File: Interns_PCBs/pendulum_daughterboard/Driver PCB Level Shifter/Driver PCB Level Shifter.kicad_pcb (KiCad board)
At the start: 2 copper layers, 69.2 x 54 mm, 69 parts, among them IC1 MAX9928FAUA+, J1 AVR-ISP-6, J2 Coil, J3 DRIVE_5V, J4 Conn_01x04, J5 DRIVE_GND, Q1 BC858W, Q2 BD911, SW1 SW_Push, U1 4081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

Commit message: Penduino Daughterboard with Level Shifter
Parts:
- removed EC3, EC4: 10u, Capacitor_SMD:CP_Elec_4x5.4
- removed J3: DRIVE_5V, Connector_Pin:Pin_D1.3mm_L11.0mm
- removed J5: DRIVE_GND, Connector_Pin:Pin_D1.3mm_L11.0mm
- added R10: 10K, Resistor_SMD:R_0805_2012Metric_Pad1.20x1.40mm_HandSolder, F.Cu at (89.9, 94.5)
- added R11: 10K, Resistor_SMD:R_0805_2012Metric_Pad1.20x1.40mm_HandSolder, F.Cu at (94.3, 85.7)
- added R12: 10K, Resistor_SMD:R_0805_2012Metric_Pad1.20x1.40mm_HandSolder, F.Cu at (89.9, 91.5)
- added R14: 10K, Resistor_SMD:R_0805_2012Metric_Pad1.20x1.40mm_HandSolder, F.Cu at (94.7, 88.6)
- U6: value AMS1117-3.3 -> SN74LVC2T45DCUR; footprint Package_TO_SOT_SMD:SOT-223-3_TabPin2 -> Package_SO:VSSOP-8_2.4x2.1mm_P0.5mm
- moved U6 41.6 mm to (84.8, 94.2)
- moved EC1 36.0 mm to (88.1, 87.1)
- moved EC2 34.8 mm to (78.2, 95.3), turned to 0 degrees
- moved U5 9.43 mm to (122.4, 103.8)
- renumbered D1_GN to D1, D2_OR to D2, D3_RD to D3, D5_RD to D5
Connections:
- EC2 pad 1: D_3.3V -> 3.3V
- J1 pad 1: LOAD_INPUT -> LOAD
- J1 pad 3: DRIVE_INPUT -> DRIVE
- U5 pad 2: D_3.3V -> 3.3V
- U6 pad 1: DRIVE_GND -> 3.3V
- U6 pad 2: PEND_3.3V -> DRIVE
- U6 pad 3: /Linear Voltage Conversion/DRIVE_5V -> LOAD
- U7 pad 6: LOAD_INPUT -> LOAD
- U7 pad 7: DRIVE_INPUT -> DRIVE
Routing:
- net DRIVE_INPUT: track 81.4 -> 2.54 mm, vias 3 -> 0
- net LOAD_INPUT: track 74.1 -> 0.00 mm, vias 2 -> 0
- net D_5V: track 41.8 -> 0.00 mm, vias 2 -> 0
- net DRIVE_GND: track 182.9 -> 141.9 mm, vias 7 -> 5
- net D_3.3V: track 93.3 -> 61.8 mm, vias 8 -> 6
- net LOAD: track 0.00 -> 30.9 mm, vias 0 -> 1
- net /Linear Voltage Conversion/DRIVE_5V: track 24.7 -> 0.00 mm
- net PEND_3.3V: track 112.1 -> 90.0 mm
- net D_GND: track 118.9 -> 107.7 mm, vias 10 -> 7
- net STUDENT_ENABLE: track 52.9 -> 51.5 mm
- net Net-(R26-Pad1): track 13.1 -> 12.0 mm
- net Net-(R30-Pad1): track 13.0 -> 12.0 mm
- net Net-(R29-Pad1): track 34.2 -> 33.4 mm
- net Net-(R28-Pad1): track 34.4 -> 33.8 mm
- net Net-(R27-Pad1): track 39.1 -> 38.5 mm
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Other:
- board text removed: "DRIVE_5V"
- board text removed: "DRIVE_GND"
- board text removed: "D_3.3V"
- board text removed: "PEND_3.3V"

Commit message: Pin update
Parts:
- added C10: 100nF, Capacitor_SMD:C_0805_2012Metric_Pad1.18x1.45mm_HandSolder, F.Cu at (130.4, 109.8)
- added C11: 100nF, Capacitor_SMD:C_0805_2012Metric_Pad1.18x1.45mm_HandSolder, F.Cu at (117.4, 110.2)
- moved U6 41.3 mm to (124.4, 106.0), turned to 180 degrees
- moved R12 41.1 mm to (126.3, 110.7)
- moved EC2 36.3 mm to (110.0, 112.9)
- moved R10 35.9 mm to (121.9, 110.7), turned to 180 degrees
- moved R14 34.2 mm to (126.7, 100.6), turned to 180 degrees
- moved R11 30.3 mm to (118.9, 103.4)
- moved EC1 24.3 mm to (110.0, 97.6), turned to 180 degrees
- moved U5 12.5 mm to (110.0, 105.5)
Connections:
- A1 pad 19: LOAD_INPUT -> DRIVE_INPUT
- A1 pad 27: DRIVE_INPUT -> LOAD_INPUT
- A1 pad 28: DRIVE_INPUT -> LOAD_INPUT
- A1 pad 5: D_5V -> 5V
- A1 pad 7: D_GND -> GND
- C1 pad 1: PEND_3.3V -> 5V
- C1 pad 2: DRIVE_GND -> GND
- C2 pad 1: PEND_3.3V -> 5V
- C2 pad 2: DRIVE_GND -> GND
- C3 pad 1: PEND_3.3V -> 5V
- C3 pad 2: DRIVE_GND -> GND
- C4 pad 1: D_3.3V -> 5V
- C4 pad 2: D_GND -> GND
- C5 pad 1: D_3.3V -> 5V
- C5 pad 2: D_GND -> GND
- C6 pad 1: D_3.3V -> 5V
- C6 pad 2: D_GND -> GND
- C7 pad 1: D_3.3V -> 5V
- C7 pad 2: D_GND -> GND
- C8 pad 1: PEND_3.3V -> 5V
- C8 pad 2: DRIVE_GND -> GND
- C9 pad 1: PEND_3.3V -> 5V
- C9 pad 2: DRIVE_GND -> GND
- D4 pad 1: DRIVE_GND -> GND
- D5 pad 1: DRIVE_GND -> GND
- EC1 pad 1: D_5V -> 5V
- EC1 pad 2: D_GND -> GND
- EC2 pad 2: D_GND -> GND
- J1 pad 2: PEND_3.3V -> 5V
- J1 pad 6: DRIVE_GND -> GND
- J2 pad 1: DRIVE_GND -> GND
- J4 pad 1: D_GND -> GND
- NT2 pad 2: PEND_3.3V -> 5V
- NT3 pad 2: DRIVE_GND -> GND
- Q1 pad 2: PEND_3.3V -> 5V
- Q2 pad 3: DRIVE_GND -> GND
- R1 pad 1: D_GND -> GND
- R10 pad 1: D_GND -> GND
- R11 pad 2: D_GND -> GND
- R12 pad 1: D_GND -> GND
- R13 pad 2: D_GND -> GND
- R14 pad 2: D_GND -> GND
- R15 pad 2: D_GND -> GND
- R17 pad 2: D_GND -> GND
- R18 pad 2: D_GND -> GND
- R19 pad 2: D_GND -> GND
- R2 pad 1: D_GND -> GND
- R20 pad 2: D_GND -> GND
- R21 pad 2: D_GND -> GND
- R22 pad 2: D_GND -> GND
- R23 pad 2: D_GND -> GND
- R24 pad 2: D_GND -> GND
- R25 pad 2: D_GND -> GND
- R26 pad 2: D_GND -> GND
- R27 pad 2: D_GND -> GND
- R28 pad 2: D_GND -> GND
- R29 pad 2: D_GND -> GND
- R3 pad 1: D_GND -> GND
- R30 pad 2: D_GND -> GND
- R31 pad 2: D_GND -> GND
- R32 pad 2: D_GND -> GND
- R33 pad 2: D_GND -> GND
- R6 pad 2: PEND_3.3V -> 5V
- R9 pad 2: D_GND -> GND
- SW1 pad 1: DRIVE_GND -> GND
- U1 pad 14: D_3.3V -> 5V
- U1 pad 7: D_GND -> GND
- U2 pad 14: D_3.3V -> 5V
- U2 pad 7: D_GND -> GND
- U3 pad 14: D_3.3V -> 5V
- U3 pad 7: D_GND -> GND
- U4 pad 14: D_3.3V -> 5V
- U4 pad 7: D_GND -> GND
- U5 pad 1: D_GND -> GND
- U5 pad 3: D_5V -> 5V
- U6 pad 1: 3.3V -> 5V
- U6 pad 4: D_GND -> GND
- U6 pad 5: D_GND -> GND
- U6 pad 8: D_5V -> 3.3V
- U7 pad 4: DRIVE_GND -> GND
- U7 pad 8: PEND_3.3V -> 5V
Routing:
- net 5V: track 0.00 -> 234.8 mm, vias 0 -> 16
- net GND: track 0.00 -> 216.4 mm, vias 0 -> 15
- net DRIVE_GND: track 141.9 -> 0.00 mm, vias 5 -> 0
- net D_GND: track 107.7 -> 0.00 mm, vias 7 -> 0
- net PEND_3.3V: track 90.0 -> 0.00 mm, vias 8 -> 0
- net DRIVE_INPUT: track 2.54 -> 76.6 mm, vias 0 -> 4
- net D_3.3V: track 61.8 -> 0.00 mm, vias 6 -> 0
- net DRIVE: track 0.00 -> 56.9 mm, vias 0 -> 2
- net LOAD_INPUT: track 0.00 -> 54.9 mm, vias 0 -> 6
- net LOAD: track 30.9 -> 62.6 mm, vias 1 -> 6
- net 3.3V: track 0.00 -> 31.0 mm
- net Net-(R25-Pad1): track 31.2 -> 43.6 mm
- net STUDENT_ENABLE: track 51.5 -> 63.4 mm, vias 4 -> 10
- net STU_LED_3: track 38.7 -> 30.0 mm
- net CURRENT_SENSE_OUT: track 47.9 -> 39.2 mm, vias 0 -> 4
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- added copper zone on B.Cu, net GND
- removed copper zone on B.Cu, net D_GND
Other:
- board text added: "5V"
- board text added: "GND"
- board text removed: "D_5V"
- board text removed: "D_GND"

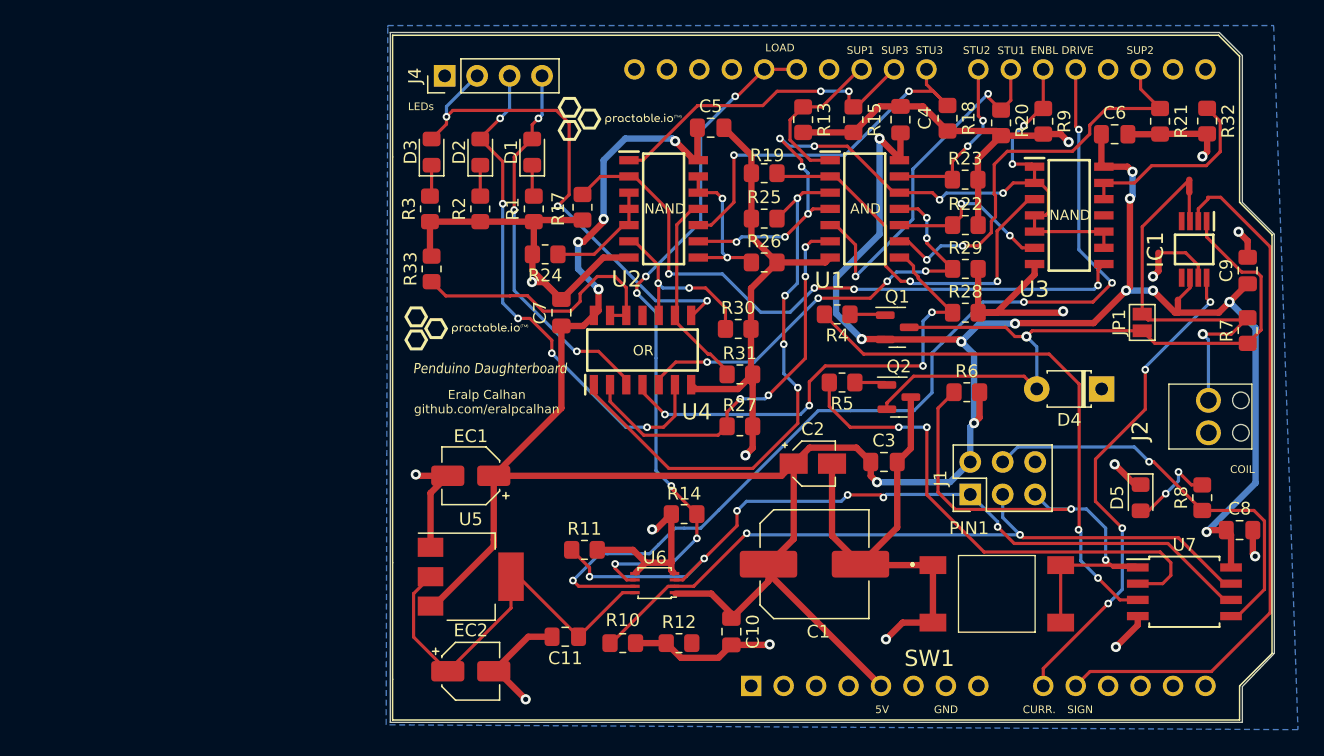
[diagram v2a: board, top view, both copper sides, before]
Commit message: Level Shifting Daughterboard
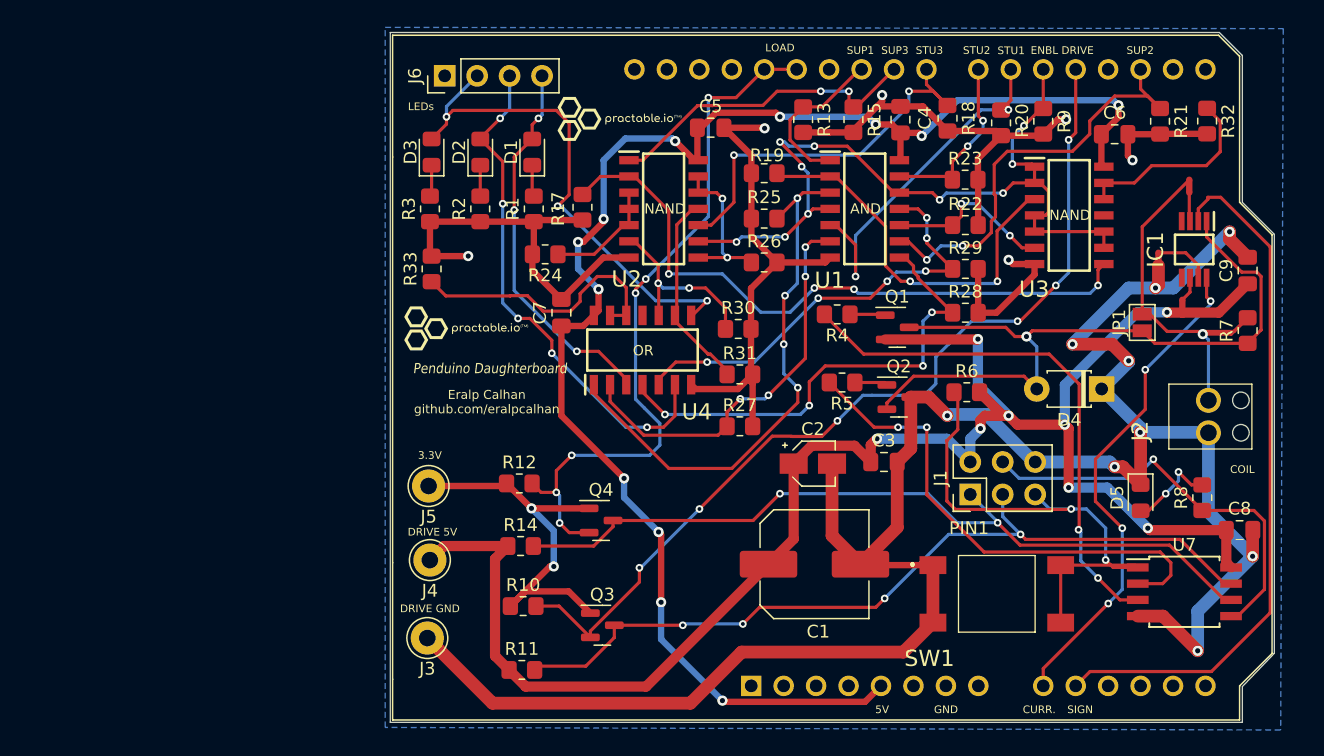
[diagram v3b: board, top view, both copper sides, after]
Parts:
- removed C10, C11: 100nF, Capacitor_SMD:C_0805_2012Metric_Pad1.18x1.45mm_HandSolder
- removed EC1, EC2: 10u, Capacitor_SMD:CP_Elec_4x5.4
- removed U5: AMS1117-3.3, Package_TO_SOT_SMD:SOT-223-3_TabPin2
- removed U6: SN74LVC2T45DCUR, Package_SO:VSSOP-8_2.4x2.1mm_P0.5mm
- added J3: DRIVE_GND, Connector_Pin:Pin_D1.3mm_L11.0mm, F.Cu at (106.6, 110.3)
- added J4: DRIVE_5V, Connector_Pin:Pin_D1.3mm_L11.0mm, F.Cu at (106.8, 104.2)
- added J5: 3.3V, Connector_Pin:Pin_D1.3mm_L11.0mm, F.Cu at (106.7, 98.4)
- added Q3: BSS138, Package_TO_SOT_SMD:SOT-23, F.Cu at (120.3, 109.3)
- added Q4: BSS138, Package_TO_SOT_SMD:SOT-23, F.Cu at (120.2, 101.1)
- R10, R11, R12, R14: value 10K -> 10k
- moved R12 17.7 mm to (113.8, 98.2)
- moved R14 13.0 mm to (113.9, 103.1), turned to 0 degrees
- moved R11 10.6 mm to (114.0, 112.8)
- moved R10 8.32 mm to (114.1, 107.8), turned to 0 degrees
- moved NT2 0.35 mm to (165.7, 84.3)
- renumbered J4 to J6
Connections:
- A1 pad 5: 5V -> D_5V
- A1 pad 7: GND -> D_GND
- C1 pad 2: GND -> DRIVE_GND
- C2 pad 2: GND -> DRIVE_GND
- C3 pad 2: GND -> DRIVE_GND
- C4 pad 1: 5V -> D_5V
- C4 pad 2: GND -> D_GND
- C5 pad 1: 5V -> D_5V
- C5 pad 2: GND -> D_GND
- C6 pad 1: 5V -> D_5V
- C6 pad 2: GND -> D_GND
- C7 pad 1: 5V -> D_5V
- C7 pad 2: GND -> D_GND
- C8 pad 1: 5V -> DRIVE_5V
- C8 pad 2: GND -> DRIVE_GND
- C9 pad 1: 5V -> DRIVE_5V
- C9 pad 2: GND -> DRIVE_GND
- D4 pad 1: GND -> DRIVE_GND
- D5 pad 1: GND -> DRIVE_GND
- J1 pad 2: 5V -> DRIVE_5V
- J1 pad 6: GND -> DRIVE_GND
- J2 pad 1: GND -> DRIVE_GND
- J6 pad 1: GND -> D_GND
- NT2 pad 2: 5V -> DRIVE_5V
- NT3 pad 2: GND -> DRIVE_GND
- Q1 pad 2: 5V -> DRIVE_5V
- Q2 pad 3: GND -> DRIVE_GND
- R1 pad 1: GND -> D_GND
- R10 pad 1: GND -> 3.3V
- R10 pad 2: DRIVE -> DRIVE_INPUT
- R11 pad 1: LOAD -> DRIVE_5V
- R11 pad 2: GND -> DRIVE
- R12 pad 1: GND -> 3.3V
- R12 pad 2: DRIVE_INPUT -> LOAD_INPUT
- R13 pad 2: GND -> D_GND
- R14 pad 1: LOAD_INPUT -> DRIVE_5V
- R14 pad 2: GND -> LOAD
- R15 pad 2: GND -> D_GND
- R17 pad 2: GND -> D_GND
- R18 pad 2: GND -> D_GND
- R19 pad 2: GND -> D_GND
- R2 pad 1: GND -> D_GND
- R20 pad 2: GND -> D_GND
- R21 pad 2: GND -> D_GND
- R22 pad 2: GND -> D_GND
- R23 pad 2: GND -> D_GND
- R24 pad 2: GND -> D_GND
- R25 pad 2: GND -> D_GND
- R26 pad 2: GND -> D_GND
- R27 pad 2: GND -> D_GND
- R28 pad 2: GND -> D_GND
- R29 pad 2: GND -> D_GND
- R3 pad 1: GND -> D_GND
- R30 pad 2: GND -> D_GND
- R31 pad 2: GND -> D_GND
- R32 pad 2: GND -> D_GND
- R33 pad 2: GND -> D_GND
- R6 pad 2: 5V -> DRIVE_5V
- R9 pad 2: GND -> D_GND
- SW1 pad 1: GND -> DRIVE_GND
- U1 pad 14: 5V -> D_5V
- U1 pad 7: GND -> D_GND
- U2 pad 14: 5V -> D_5V
- U2 pad 7: GND -> D_GND
- U3 pad 14: 5V -> D_5V
- U3 pad 7: GND -> D_GND
- U4 pad 14: 5V -> D_5V
- U4 pad 7: GND -> D_GND
- U7 pad 4: GND -> DRIVE_GND
- U7 pad 8: 5V -> DRIVE_5V
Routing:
- net 5V: track 234.8 -> 0.00 mm, vias 16 -> 0
- net GND: track 216.4 -> 0.00 mm, vias 15 -> 0
- net DRIVE_GND: track 0.00 -> 169.6 mm, vias 0 -> 9
- net DRIVE_5V: track 0.00 -> 138.4 mm, vias 0 -> 8
- net D_GND: track 0.00 -> 122.5 mm, vias 0 -> 6
- net D_5V: track 0.00 -> 118.7 mm, vias 0 -> 12
- net DRIVE: track 56.9 -> 64.3 mm, vias 2 -> 4
- net DRIVE_INPUT: track 76.6 -> 72.8 mm, vias 4 -> 6
- net LOAD_INPUT: track 54.9 -> 56.1 mm
- net LOAD_OUT: track 40.6 -> 39.5 mm
- net SUP_LED_2: track 33.1 -> 34.1 mm
- net Net-(R25-Pad1): track 43.6 -> 42.7 mm
- net Net-(J2-Pad2): track 29.7 -> 30.5 mm
- net STU_LED_3: track 30.0 -> 30.6 mm
- net Net-(R28-Pad1): track 37.8 -> 37.3 mm
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- added copper zone on B.Cu, net D_GND
- removed copper zone on B.Cu, net GND
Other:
- board text added: "3.3V"
- board text added: "DRIVE 5V"
- board text added: "DRIVE GND"

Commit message: Truss Test
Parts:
- renumbered U7 to U5
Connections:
- C1 pad 1: 5V -> DRIVE_5V
- C2 pad 1: 5V -> DRIVE_5V
- C3 pad 1: 5V -> DRIVE_5V
